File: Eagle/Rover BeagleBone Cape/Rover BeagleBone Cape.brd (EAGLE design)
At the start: 86.4 x 54.6 mm, 31 parts, among them IC1 TXB0108TSSOP, IC2 VREG-3TO-263, M0 M-1X05PTH, M1 M-1X05PTH, M2 M-1X05PTH, M3 M-1X05PTH, M4 M-1X05PTH, M5 M-1X05PTH, U2 MCP9808MSOP, U3 HTU21DSMD, U4 BMP180, U6 Hydrogen, U7 Carbon Monoxide, U8 LPG, U9 Methane

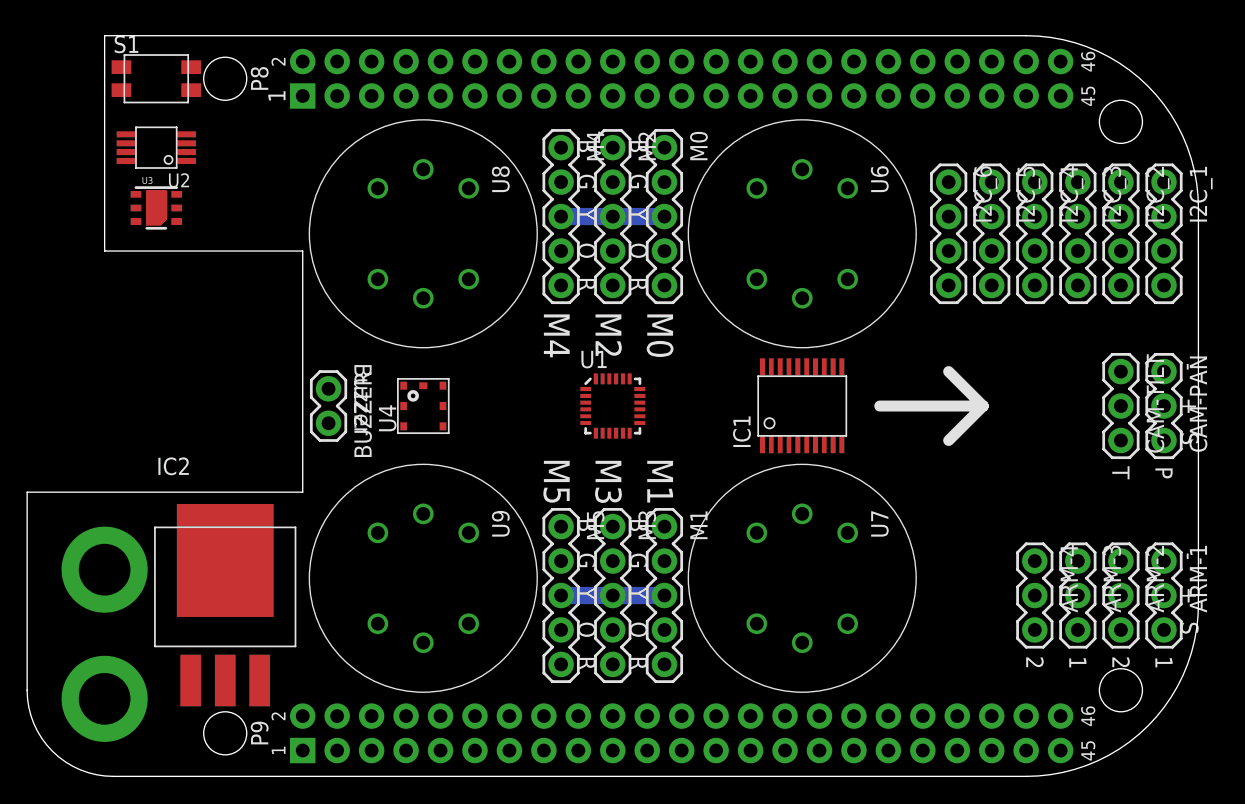
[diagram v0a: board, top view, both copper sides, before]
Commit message: Added preliminary motor controller code
Added Arduino code and PCB revisions
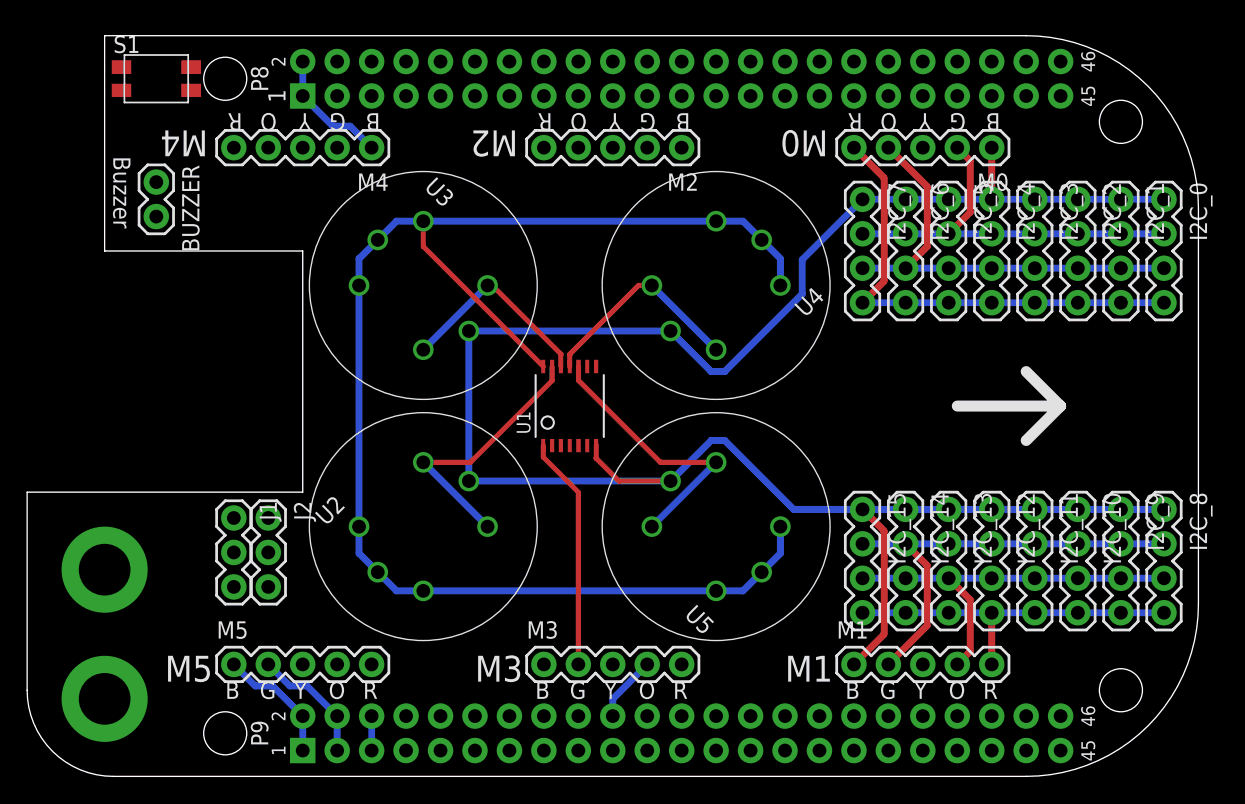
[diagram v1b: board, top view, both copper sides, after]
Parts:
- removed ARM-1, ARM-2, ARM-3, ARM-4, CAM-PAN, CAM-TILT: M-1X03PTH, Jordi:M-1X03-0.1-PTH
- removed IC1: TXB0108TSSOP, Jordi:TSSOP-20
- removed IC2: VREG-3TO-263, Jordi:TO-263-3
- removed U6: Hydrogen, Jordi:MQ-X
- removed U7: Carbon Monoxide, Jordi:MQ-X
- removed U8: LPG, Jordi:MQ-X
- removed U9: Methane, Jordi:MQ-X
- added I2C_0: IMU, Jordi:M-1X04-0.1-PTH
- added I2C_10, I2C_11, I2C_12, I2C_13, I2C_14, I2C_15, I2C_7: 1X04M-0.1-PTH, Jordi:M-1X04-0.1-PTH
- added I2C_8: IR Temp, Jordi:M-1X04-0.1-PTH
- added I2C_9: Color, Jordi:M-1X04-0.1-PTH
- added J1, J2: (no value), Jordi:M-1X03-0.1-PTH
- added U5: Methane, Jordi:MQ-X
- BUZZER: value M-1X02PTH -> (none)
- I2C_1: value IR Temp -> Gas
- I2C_2: value Color -> Optical Dust
- I2C_3: value Light -> Temperature
- I2C_4: value Optical Dust -> Humidity
- I2C_5: value Ph -> Barometric
- I2C_6: value M-1X04PTH -> Light
- M0, M1, M2, M3, M4, M5: value M-1X05PTH -> (none)
- U1: device SparkFun-Sensors:QFN-24-NP -> SparkFun-DigitalIC:TSSOP14
- U2: value MCP9808MSOP -> Hydrogen; device Jordi:MSOP-8 -> Jordi:MQ-X
- U3: value HTU21DSMD -> Carbon Monoxide; device SparkFun-Sensors:HTU21D -> Jordi:MQ-X
- U4: value BMP180 -> LPG; device SparkFun-Sensors:BMP180 -> Jordi:MQ-X
- moved U2 34.2 mm to (29.2, 18.4), turned to 45 degrees
- moved U4 23.3 mm to (50.8, 36.2), turned to 225 degrees
- moved U3 20.5 mm to (29.2, 36.2), turned to 315 degrees
- moved BUZZER 19.8 mm to (9.53, 42.5)
- moved M0 19.7 mm to (66.0, 46.4), turned to 180 degrees
- moved M1 19.7 mm to (66.0, 8.26), turned to 0 degrees
- moved M4 19.7 mm to (20.3, 46.4), turned to 180 degrees
- moved M5 19.7 mm to (20.3, 8.26), turned to 0 degrees
- moved M3 5.08 mm to (43.2, 8.26), turned to 0 degrees
- moved M2 5.08 mm to (43.2, 46.4), turned to 180 degrees
- moved I2C_5 3.42 mm to (67.9, 38.7)
- moved I2C_1 3.42 mm to (80.6, 38.7)
- moved I2C_2 3.42 mm to (77.5, 38.7)
- moved I2C_3 3.42 mm to (74.3, 38.7)
- moved I2C_4 3.42 mm to (71.1, 38.7)
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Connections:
- removed net IN: IC2.1
- removed net OUT: IC2.3
- net +3V3: now also I2C_0.2, I2C_10.2, I2C_11.2, I2C_12.2, I2C_13.2, I2C_14.2, I2C_15.2, I2C_7.2, I2C_8.2, I2C_9.2, U1.1; no longer IC1.2, U1.13, U1.3, U1.8, U2.8, U3.VDD, U4.2, U4.3
- net +5V: now also J1.2, J2.2, U1.14, U2.A1, U2.A2, U2.HA, U3.A1, U3.A2, U3.HA, U4.A1, U4.A2, U4.HA, U5.A1, U5.A2, U5.HA; no longer ARM-1.2, ARM-2.2, ARM-3.2, ARM-4.2, CAM-PAN.2, CAM-TILT.2, IC1.19, U6.A1, U6.A2, U6.HA, U7.A1, U7.A2, U7.HA, U8.A1, U8.A2, U8.HA, U9.A1, U9.A2, U9.HA
- net G1: now also U1.13, U2.B1, U2.B2; no longer IC1.20, U6.B1, U6.B2
- net G2: now also U1.12, U3.B1, U3.B2; no longer IC1.18, U7.B1, U7.B2
- net G3: now also U1.11, U4.B1, U4.B2; no longer IC1.17, U8.B1, U8.B2
- net G4: now also U1.10, U5.B1, U5.B2; no longer IC1.16, U9.B1, U9.B2
- net GND: now also I2C_0.1, I2C_10.1, I2C_11.1, I2C_12.1, I2C_13.1, I2C_14.1, I2C_15.1, I2C_7.1, I2C_8.1, I2C_9.1, J1.3, J2.3, U1.7, U2.HB, U3.HB, U4.HB, U5.HB; no longer ARM-1.1, ARM-2.1, ARM-3.1, ARM-4.1, CAM-PAN.1, CAM-TILT.1, IC1.11, IC2.2, IC2.4, U1.15, U1.17, U1.18, U2.4, U3.7, U3.GND, U4.7, U6.HB, U7.HB, U8.HB, U9.HB
- net SCL: now also I2C_0.4, I2C_1.4, I2C_10.4, I2C_11.4, I2C_12.4, I2C_13.4, I2C_14.4, I2C_15.4, I2C_2.4, I2C_3.4, I2C_4.4, I2C_5.4, I2C_6.4, I2C_7.4, I2C_8.4, I2C_9.4; no longer I2C_1.3, I2C_2.3, I2C_3.3, I2C_4.3, I2C_5.3, I2C_6.3, U1.23, U2.2, U3.SCK, U4.5
- net SDA: now also I2C_0.3, I2C_1.3, I2C_10.3, I2C_11.3, I2C_12.3, I2C_13.3, I2C_14.3, I2C_15.3, I2C_2.3, I2C_3.3, I2C_4.3, I2C_5.3, I2C_6.3, I2C_7.3, I2C_8.3, I2C_9.3; no longer I2C_1.4, I2C_2.4, I2C_3.4, I2C_4.4, I2C_5.4, I2C_6.4, U1.24, U2.1, U3.DATA, U4.6
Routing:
- net GND: track 0.00 -> 167.2 mm, vias 0 -> 1
- net +5V: track 0.00 -> 109.3 mm
- net +3V3: track 0.00 -> 89.0 mm
- net SDA: track 0.00 -> 67.4 mm
- net SCL: track 0.00 -> 61.3 mm
- net G4: track 0.00 -> 20.4 mm
- net G1: track 0.00 -> 19.7 mm
- net G3: track 0.00 -> 15.8 mm
- net VCC: track 15.2 -> 0.00 mm, vias 0 -> 1
- net G2: track 0.00 -> 15.1 mm
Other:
- board text removed: "+"
- board text removed: "-"
- board text removed: "1"
- board text removed: "2"
- board text removed: "P"
- board text removed: "S"
- board text removed: "T"
